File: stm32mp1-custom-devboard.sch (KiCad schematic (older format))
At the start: 11 parts, among them P1 Main Power Supply, U10 APX803D-29SRG-7

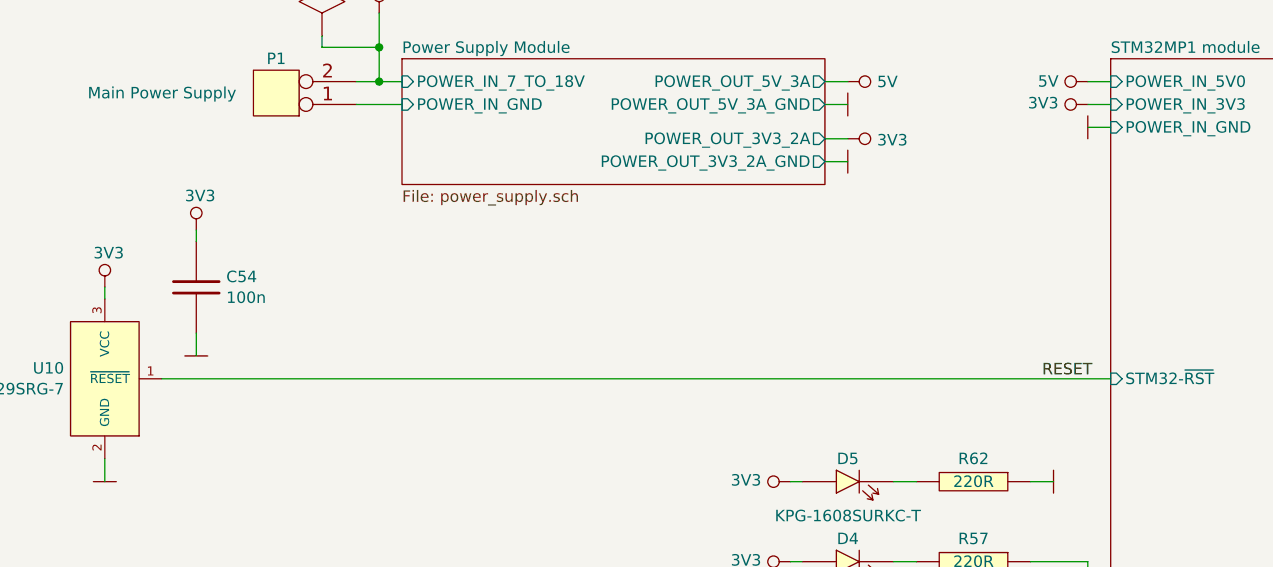
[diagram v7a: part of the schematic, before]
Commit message: Added missing URLs in BOM
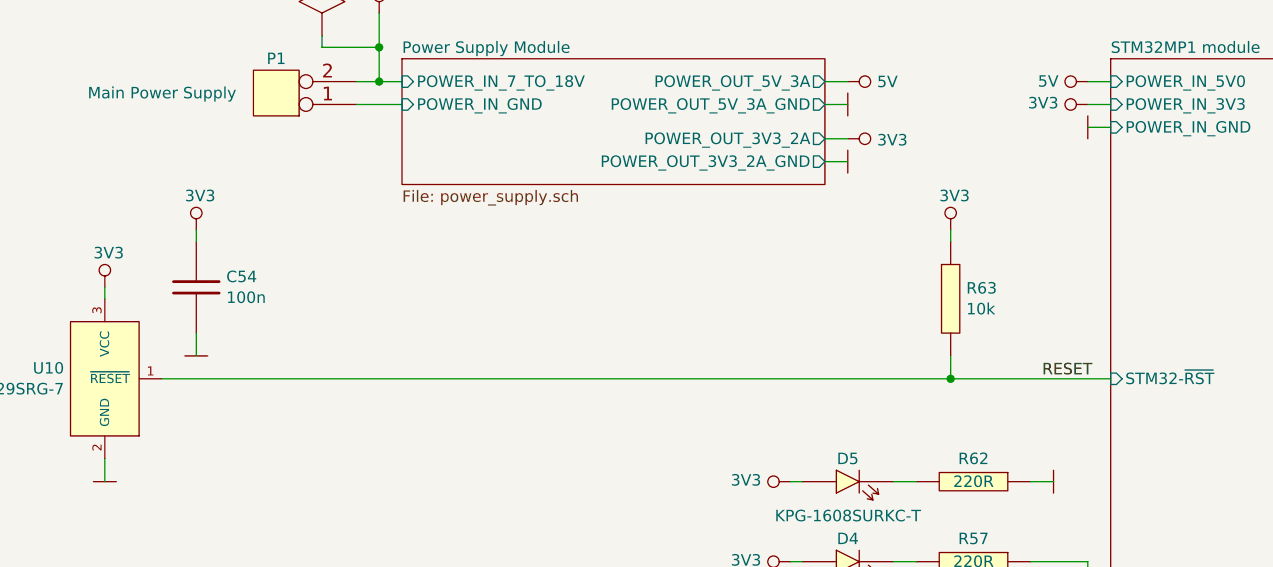
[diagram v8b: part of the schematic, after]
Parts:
- added R63: 10k, Resistor_Smd_0603:10k_0603, symbol Resistors_Smd0603:10k
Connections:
- net 3V3: now also R63.1
- net RESET: now also R63.2
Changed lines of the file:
@@
 $EndComp
 Wire Wire Line
-	7500 3000 3350 3000
+	7500 3000 6800 3000
 $Comp
 L power:GND #PWR0188
@@
 	1    0    0    -1
 $EndComp
+$Comp
+L Resistors_Smd0603:10k R63
+U 1 1 600B850B
+P 6800 2650
+F 0 "R63" H 6868 2696 50  0000 L CNN
+F 1 "10k" H 6868 2605 50  0000 L CNN
+F 2 "Resistor_Smd_0603:10k_0603" H 6800 2650 60  0001 C CNN
+F 3 "Resistors/Smd_0603/Components_Documentation/Vishay_Resistors_SM0603.pdf" H 6800 2650 60  0001 C CNN
+F 4 "ROYAL OHM" H 6800 2650 50  0001 C CNN "Manufacturer"
+F 5 "0603SAJ0103T5E" H 6800 2650 50  0001 C CNN "Manufacturer Part Number"
+F 6 "TME" H 6800 2650 50  0001 C CNN "Supplier"
+F 7 "SMD0603-10K" H 6800 2650 50  0001 C CNN "Supplier Part Number"
+F 8 "https://www.tme.eu/pl/details/smd0603-10k/rezystory-smd-0603/royal-ohm/0603saj0103t5e/" H 6800 2650 50  0001 C CNN "URL"
+F 9 "0,04560" H 6800 2650 50  0001 C CNN "Price@1pc"
+F 10 "0,01111" H 6800 2650 50  0001 C CNN "Price@1000pcs"
+F 11 "MW" H 6800 2650 50  0001 C CNN "Developer"
+F 12 "0603" H 6800 2650 50  0001 C CNN "Package"
+	1    6800 2650
+	1    0    0    -1
+$EndComp
+Wire Wire Line
+	6800 2900 6800 3000
+Connection ~ 6800 3000
+Wire Wire Line
+	6800 3000 3350 3000
+$Comp
+L power:3V3 #PWR0197
+U 1 1 600C4C98
+P 6800 2350
+F 0 "#PWR0197" H 6800 2450 40  0001 C CNN
+F 1 "3V3" H 6750 2500 50  0000 L CNN
+F 2 "" H 6800 2350 60  0000 C CNN
+F 3 "" H 6800 2350 60  0000 C CNN
+	1    6800 2350
+	1    0    0    -1
+$EndComp
+Wire Wire Line
+	6800 2400 6800 2350
 $EndSCHEMATC
